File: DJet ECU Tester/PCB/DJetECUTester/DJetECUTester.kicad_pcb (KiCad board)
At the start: 2 copper layers, 162 x 90 mm, 155 parts, among them J1 ISP, J10 ECU3, J2 ECU1, J3 USB_B_Mini, J4 12V 4A IN (5.5/2.5), J5 12V IN, J6 MPS, J7 Conn_01x01, J8 Conn_01x01, J9 ECU2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

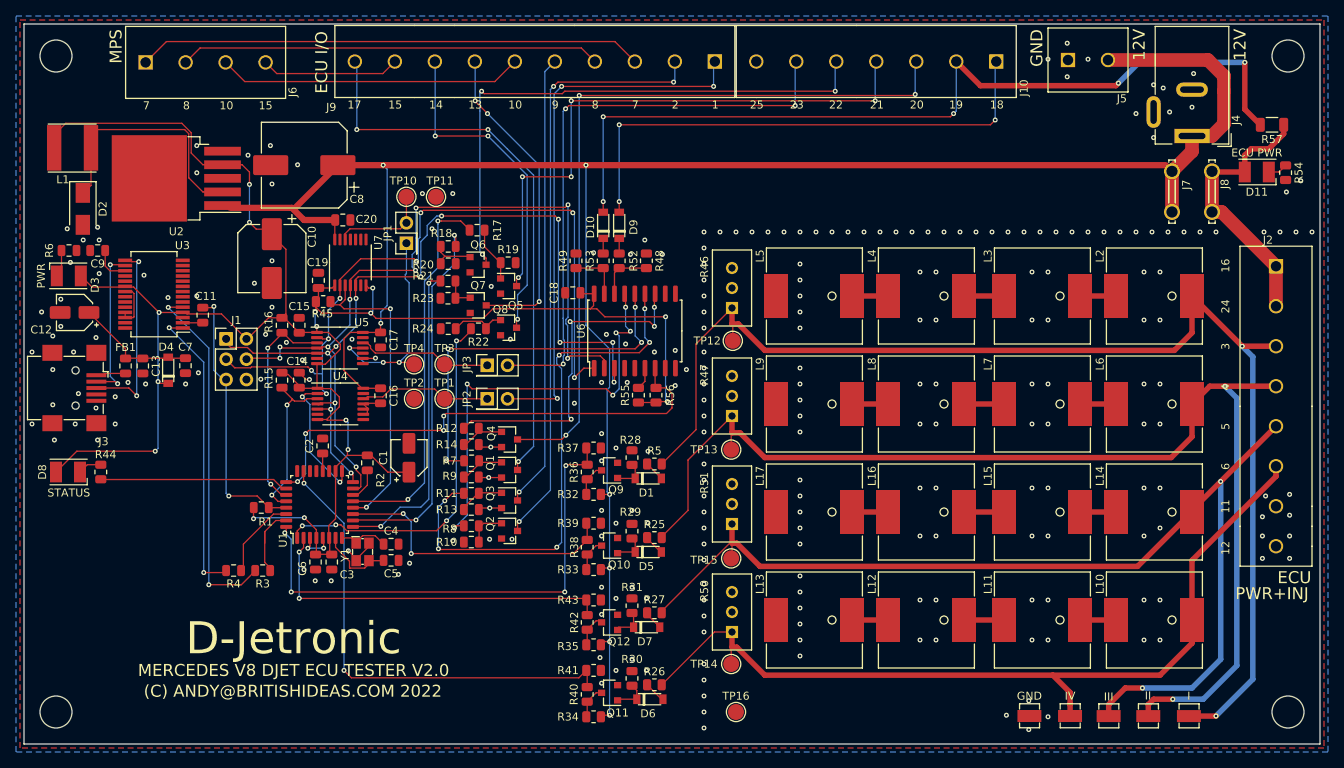
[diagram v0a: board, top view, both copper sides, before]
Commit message: Changed start signal from ECU output to ECU input.
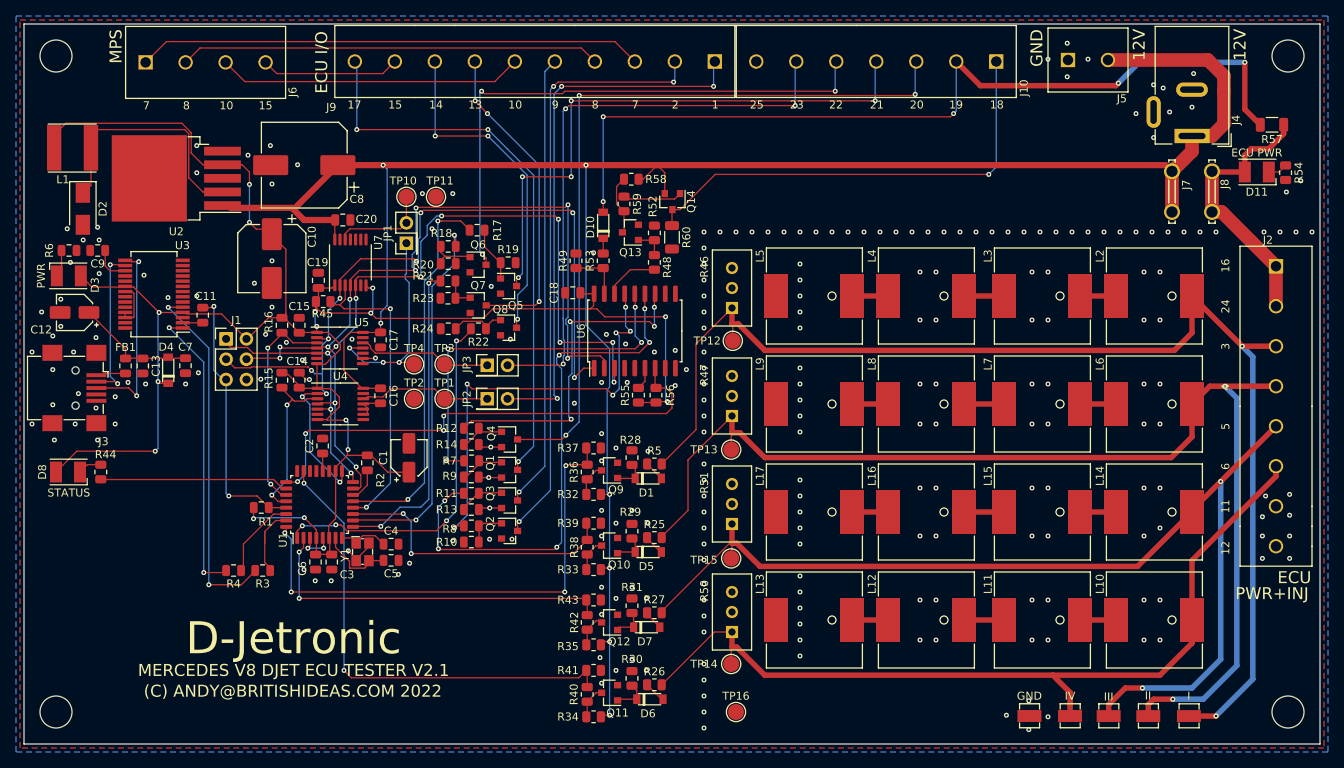
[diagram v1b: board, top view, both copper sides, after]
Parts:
- removed D9: MBR0520LT1G, Britishideas:SOD-123
- added Q13: MMBT2222ALT1G, Package_TO_SOT_SMD:SOT-23, F.Cu at (249.8, 81.0)
- added Q14: MMBT3906LT1G, Package_TO_SOT_SMD:SOT-23, F.Cu at (255.1, 77.2)
- added R58: 10k, Resistor_SMD:R_0805_2012Metric, F.Cu at (249.9, 74.4)
- added R59: 1k, Resistor_SMD:R_0805_2012Metric, F.Cu at (249.0, 77.5)
- added R60: 680, Resistor_SMD:R_1206_3216Metric, F.Cu at (255.0, 81.7)
- R48: value 4k2 -> 1k
- moved R52 5.61 mm to (252.8, 81.1)
- moved R48 1.02 mm to (252.8, 84.8)
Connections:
- R48 pad 1: GND -> Net-(Q13-Pad1)
- R52 pad 1: /MCU_START-18 -> Net-(Q13-Pad1)
- R52 pad 2: Net-(D9-Pad1) -> GND
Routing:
- net /ECU_START-18: track 65.5 -> 57.9 mm, vias 3 -> 1
- net Net-(Q13-Pad3): track 0.00 -> 7.50 mm
- net Net-(Q14-Pad1): track 0.00 -> 7.41 mm
- net +12V: track 276.1 -> 283.1 mm
- net Net-(Q13-Pad1): track 0.00 -> 3.87 mm
- net Net-(D9-Pad1): track 1.89 -> 0.00 mm
- net GND: vias 256 -> 253
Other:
- board text added: "MERCEDES V8 DJET ECU TESTER V2.1"
- board text removed: "MERCEDES V8 DJET ECU TESTER V2.0"

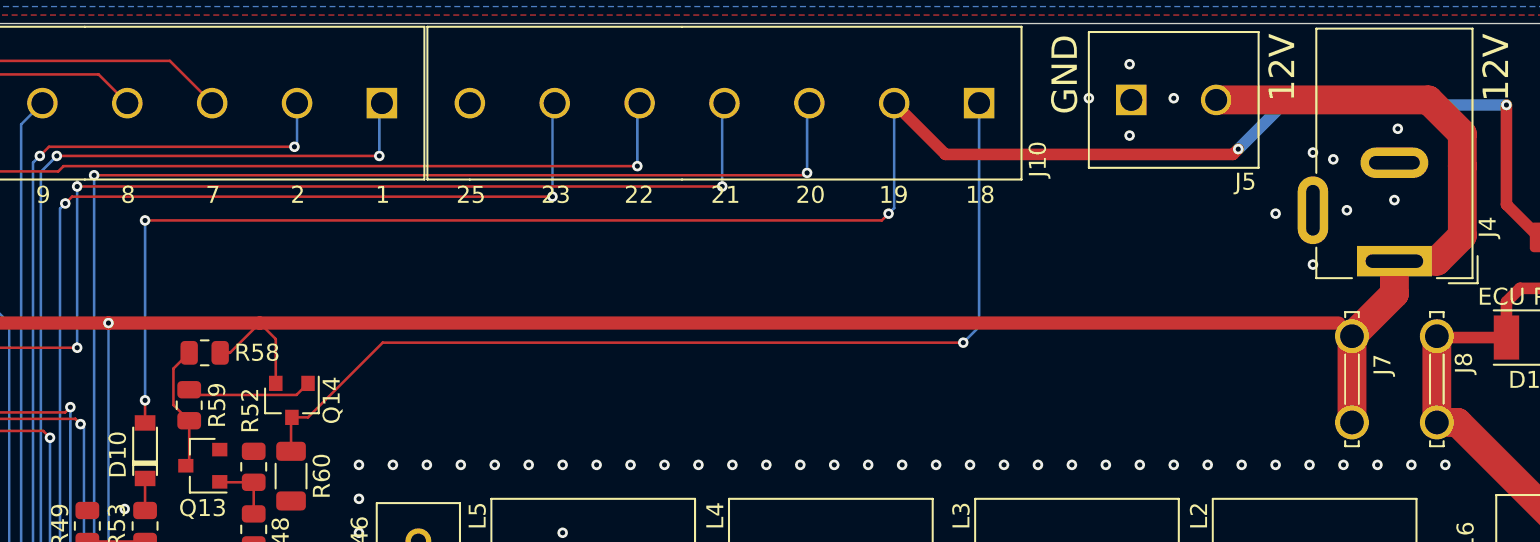
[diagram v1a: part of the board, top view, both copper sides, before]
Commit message: Added connector for cooling fan.
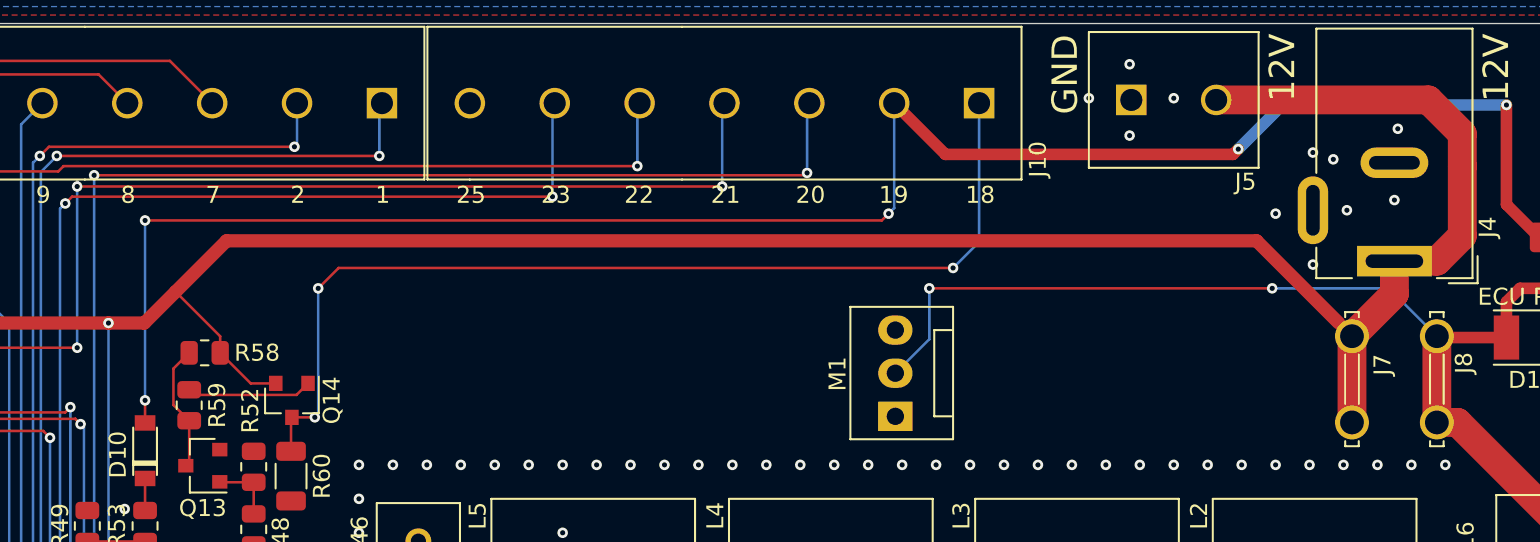
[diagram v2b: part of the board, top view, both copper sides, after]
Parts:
- added M1: Fan_3pin, Connector:FanPinHeader_1x03_P2.54mm_Vertical, F.Cu at (290.6, 78.1)
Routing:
- net /ECU_PWR: track 34.2 -> 71.1 mm, vias 0 -> 2
- net +12V: track 283.1 -> 288.8 mm
- net /ECU_START-18: track 57.9 -> 59.3 mm, vias 1 -> 3

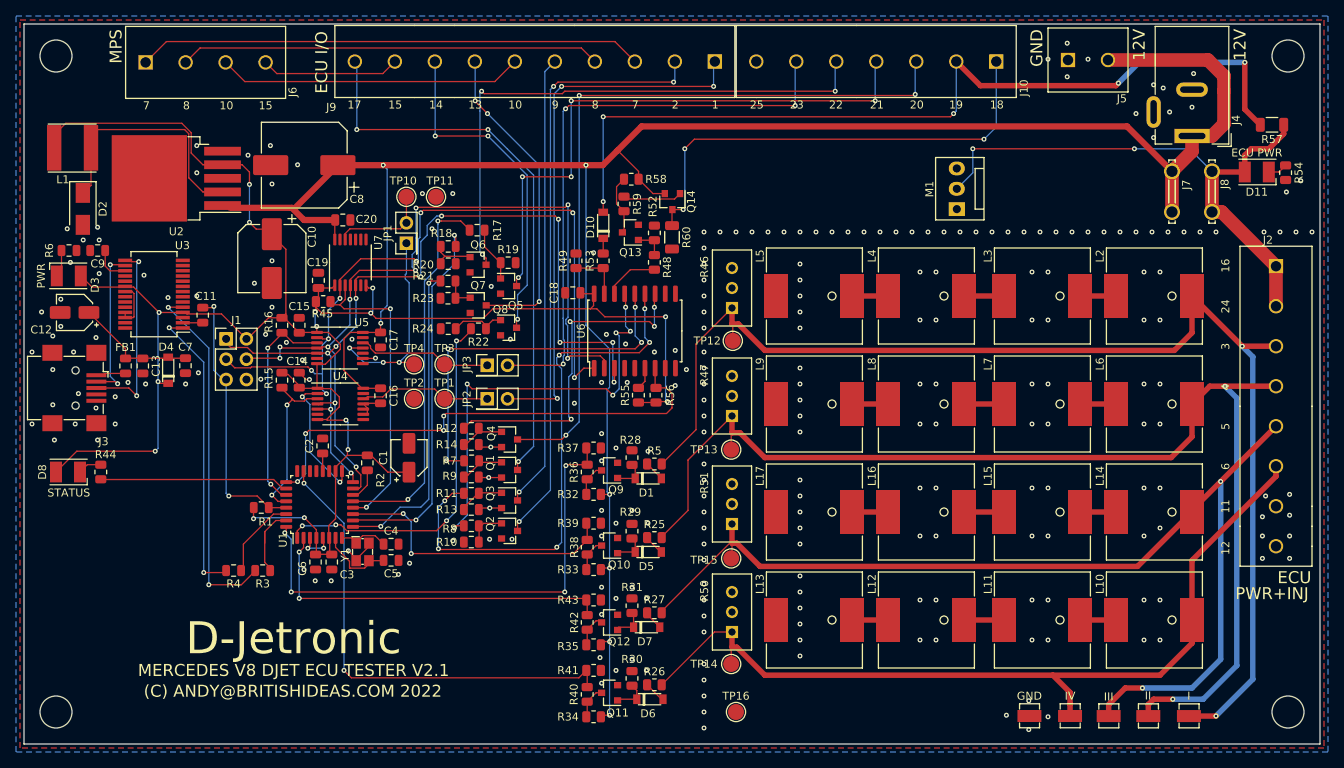
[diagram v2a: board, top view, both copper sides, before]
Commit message: Added screw block for connecting ECU power switch.
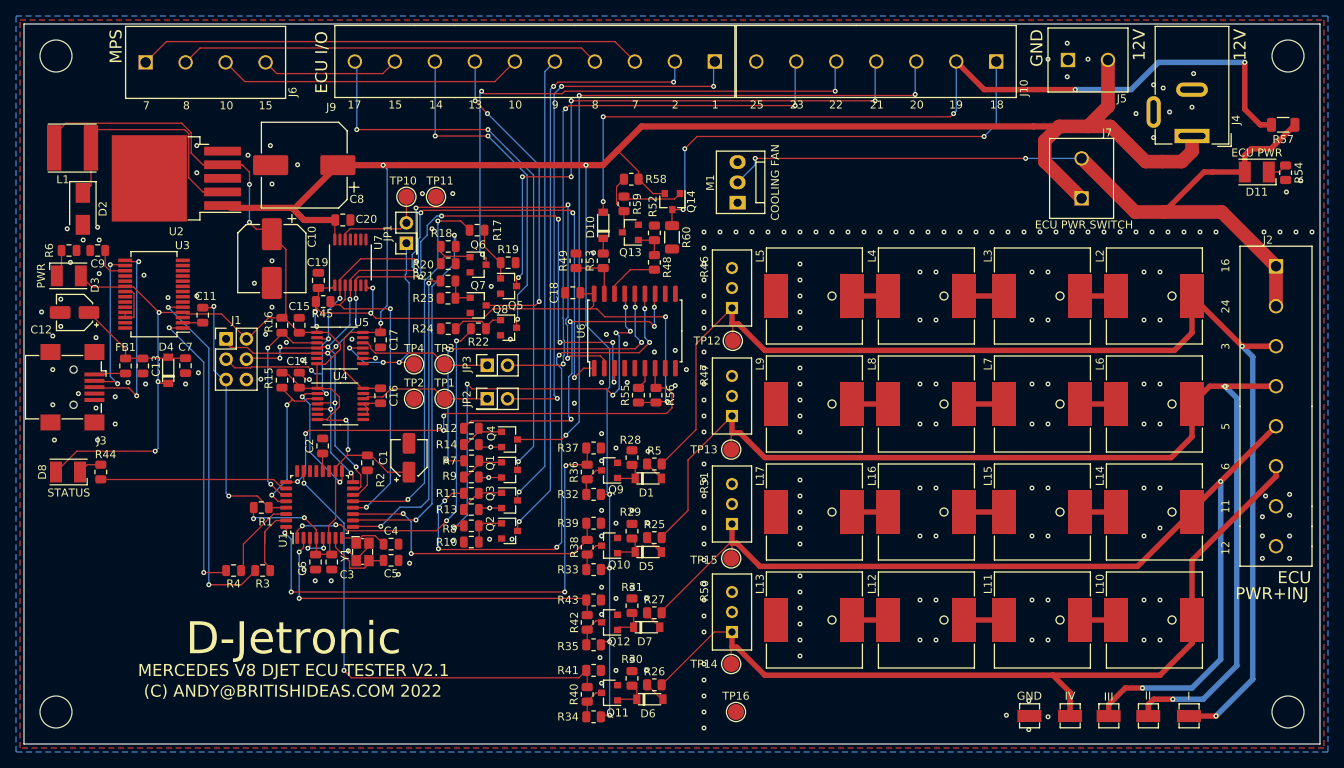
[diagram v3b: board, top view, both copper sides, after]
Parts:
- removed J8: Conn_01x01, Britishideas:tabconnector-63849-1
- J7: value Conn_01x01 -> ECU PWR SWITCH; footprint Britishideas:tabconnector-63849-1 -> Britishideas:PhoenixContact_COMBICON_MKDSN_2
- moved M1 27.4 mm to (263.2, 77.3)
- moved J7 11.4 mm to (306.2, 76.8)
- moved R57 1.40 mm to (331.4, 67.6)
- moved J3 0.27 mm to (180.2, 100.4)
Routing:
- net /ECU_PWR: track 71.1 -> 101.7 mm
- net +12V: track 288.8 -> 277.7 mm
- net /ECU_FUELPUMPRELAY-19: track 109.7 -> 111.5 mm
- net GND: vias 253 -> 249
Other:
- board text added: "COOLING FAN"
- board text added: "ECU PWR SWITCH"

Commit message: Added more robust test points. Added GPIO connector.
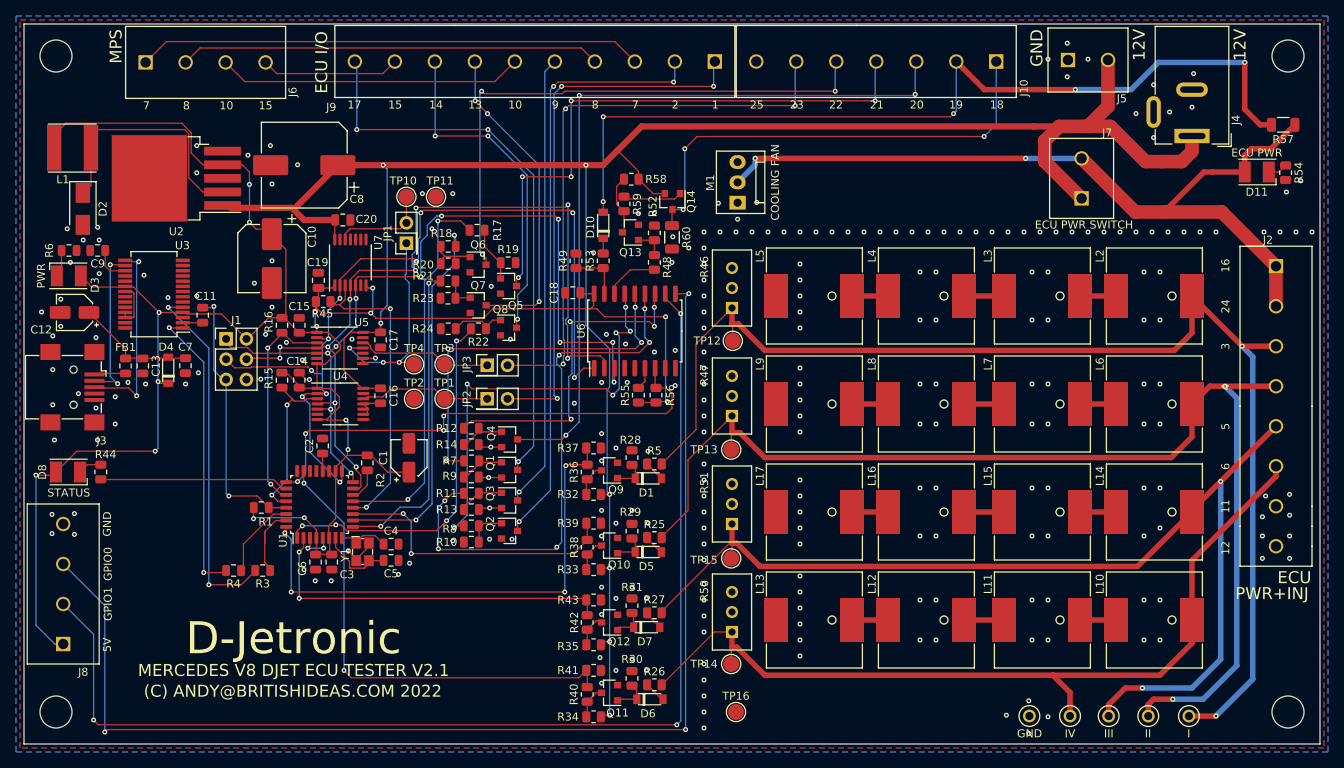
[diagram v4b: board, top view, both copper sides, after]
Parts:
- added J8: GPIO, Britishideas:PhoenixContact_COMBICON_PT_4, F.Cu at (178.9, 132.5)
- TP5, TP6, TP7, TP8: value 5194TR -> 5003; footprint Britishideas:5190TR-Colored-Test-Point -> Britishideas:Keystone-Minature-Test-Point-Colored-500x-511x
- TP9: value 5195TR -> 5115; footprint Britishideas:5190TR-Colored-Test-Point -> Britishideas:Keystone-Minature-Test-Point-Colored-500x-511x
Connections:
- U6 pad 10: (no net) -> Net-(J8-Pad3)
- U6 pad 11: (no net) -> Net-(J8-Pad2)
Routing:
- net Net-(J8-Pad3): track 0.00 -> 152.2 mm, vias 0 -> 3
- net Net-(J8-Pad2): track 0.00 -> 144.1 mm, vias 0 -> 3
- net +5V: track 254.7 -> 280.5 mm, vias 15 -> 16
- net GND: vias 249 -> 259
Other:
- board text added: "5V"
- board text added: "GPIO0"
- board text added: "GPIO1"

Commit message: Added ground vias. Regenerated 3D model of PCB. Minor improvement to case top.
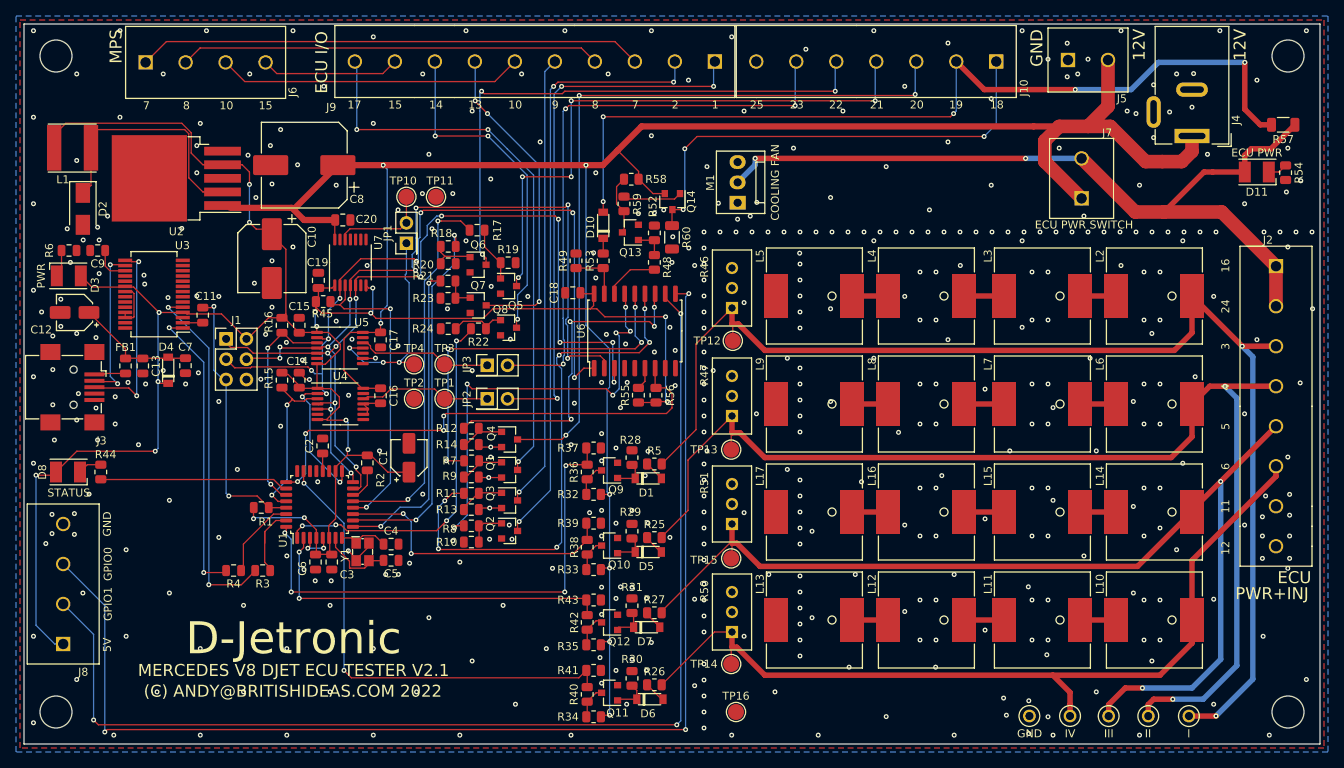
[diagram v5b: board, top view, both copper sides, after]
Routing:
- net GND: vias 259 -> 472
